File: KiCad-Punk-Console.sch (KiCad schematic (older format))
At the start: 5 parts

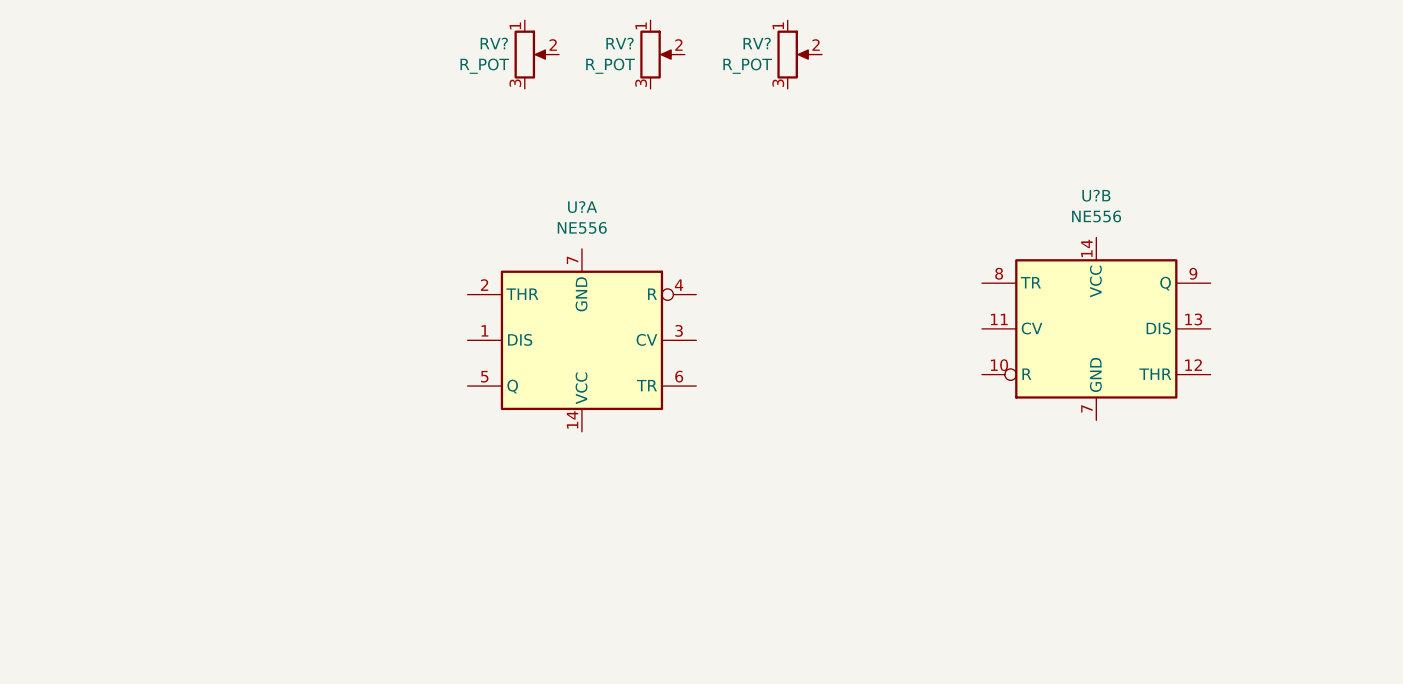
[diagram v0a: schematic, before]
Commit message: placed symbols
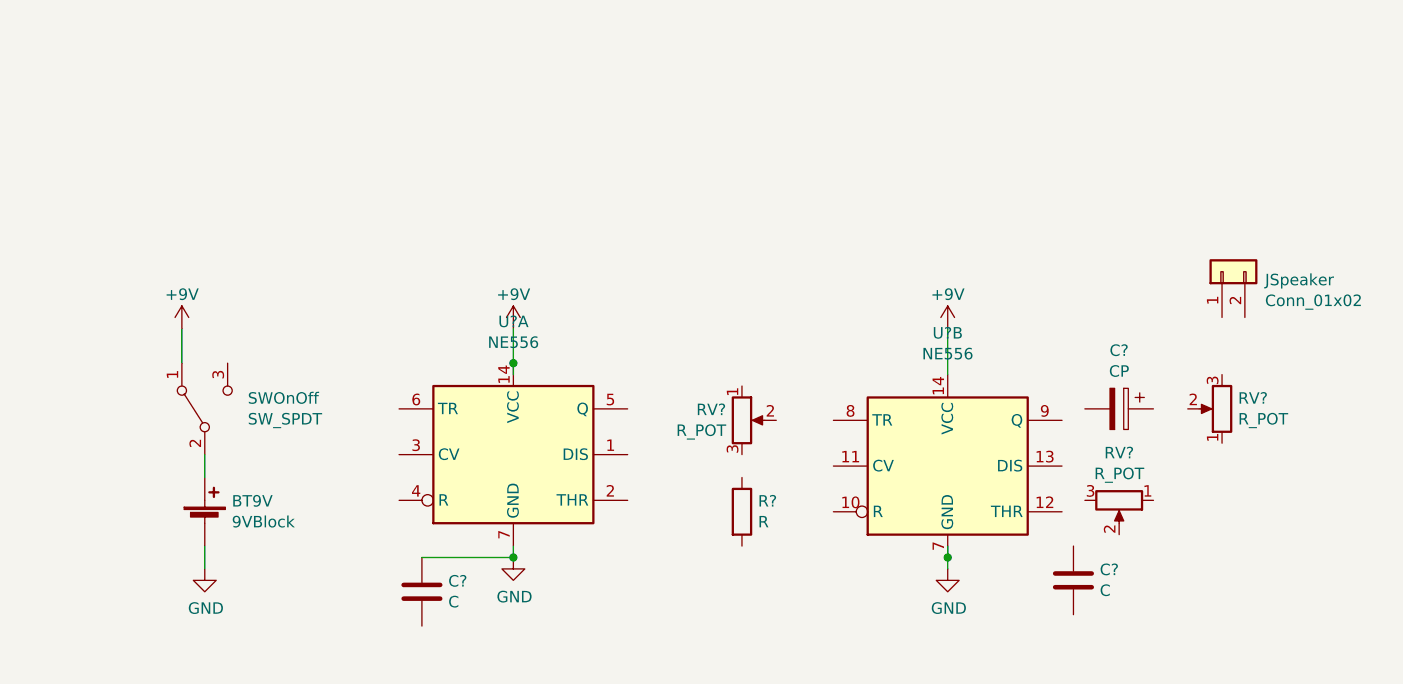
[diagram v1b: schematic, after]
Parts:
- added BT9V: 9VBlock, symbol Device:Battery_Cell
- added C? (x2): C, symbol Device:C
- added C?: CP, symbol Device:CP
- added JSpeaker: Conn_01x02, symbol Connector_Generic:Conn_01x02
- added R?: R, symbol Device:R
- added SWOnOff: SW_SPDT, symbol Switch:SW_SPDT
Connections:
- net labels added: +9V, GND
- wire segments 0 -> 10
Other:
- moved on the sheet: RV?, U?A, U?B
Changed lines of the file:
@@
 L Timer:NE556 U?
 U 1 1 5D8120BC
-P 5100 3000
-F 0 "U?" H 5100 2419 50  0000 C CNN
-F 1 "NE556" H 5100 2510 50  0000 C CNN
-F 2 "" H 5100 3000 50  0001 C CNN
-F 3 "http://www.ti.com/lit/ds/symlink/ne556.pdf" H 5100 3000 50  0001 C CNN
-	1    5100 3000
-	-1   0    0    1
+P 4800 3500
+F 0 "U?" H 4800 4081 50  0000 C CNN
+F 1 "NE556" H 4800 3990 50  0000 C CNN
+F 2 "" H 4800 3500 50  0001 C CNN
+F 3 "http://www.ti.com/lit/ds/symlink/ne556.pdf" H 4800 3500 50  0001 C CNN
+	1    4800 3500
+	1    0    0    -1
 $EndComp
 $Comp
 L Timer:NE556 U?
 U 2 1 5D81293A
-P 7350 2950
-F 0 "U?" H 7350 3531 50  0000 C CNN
-F 1 "NE556" H 7350 3440 50  0000 C CNN
-F 2 "" H 7350 2950 50  0001 C CNN
-F 3 "http://www.ti.com/lit/ds/symlink/ne556.pdf" H 7350 2950 50  0001 C CNN
-	2    7350 2950
+P 6700 3550
+F 0 "U?" H 6700 4131 50  0000 C CNN
+F 1 "NE556" H 6700 4040 50  0000 C CNN
+F 2 "" H 6700 3550 50  0001 C CNN
+F 3 "http://www.ti.com/lit/ds/symlink/ne556.pdf" H 6700 3550 50  0001 C CNN
+	2    6700 3550
 	1    0    0    -1
 $EndComp
@@
 L Device:R_POT RV?
 U 1 1 5D8204BB
-P 4850 1750
-F 0 "RV?" H 4781 1796 50  0000 R CNN
-F 1 "R_POT" H 4781 1705 50  0000 R CNN
-F 2 "" H 4850 1750 50  0001 C CNN
-F 3 "~" H 4850 1750 50  0001 C CNN
-	1    4850 1750
+P 5800 3350
+F 0 "RV?" H 5731 3396 50  0000 R CNN
+F 1 "R_POT" H 5731 3305 50  0000 R CNN
+F 2 "" H 5800 3350 50  0001 C CNN
+F 3 "~" H 5800 3350 50  0001 C CNN
+	1    5800 3350
 	1    0    0    -1
 $EndComp
@@
 L Device:R_POT RV?
 U 1 1 5D821740
-P 5400 1750
-F 0 "RV?" H 5331 1796 50  0000 R CNN
-F 1 "R_POT" H 5331 1705 50  0000 R CNN
-F 2 "" H 5400 1750 50  0001 C CNN
-F 3 "~" H 5400 1750 50  0001 C CNN
-	1    5400 1750
-	1    0    0    -1
+P 7900 3300
+F 0 "RV?" H 7830 3254 50  0000 R CNN
+F 1 "R_POT" H 7830 3345 50  0000 R CNN
+F 2 "" H 7900 3300 50  0001 C CNN
+F 3 "~" H 7900 3300 50  0001 C CNN
+	1    7900 3300
+	-1   0    0    1
 $EndComp
 $Comp
 L Device:R_POT RV?
 U 1 1 5D8219B1
-P 6000 1750
-F 0 "RV?" H 5931 1796 50  0000 R CNN
-F 1 "R_POT" H 5931 1705 50  0000 R CNN
-F 2 "" H 6000 1750 50  0001 C CNN
-F 3 "~" H 6000 1750 50  0001 C CNN
-	1    6000 1750
-	1    0    0    -1
-$EndComp
+P 7450 3700
+F 0 "RV?" V 7243 3700 50  0000 C CNN
+F 1 "R_POT" V 7334 3700 50  0000 C CNN
+F 2 "" H 7450 3700 50  0001 C CNN
+F 3 "~" H 7450 3700 50  0001 C CNN
+	1    7450 3700
+	0    1    1    0
+$EndComp
+$Comp
+L Device:R R?
+U 1 1 5D8233A2
+P 5800 3750
+F 0 "R?" H 5870 3796 50  0000 L CNN
+F 1 "R" H 5870 3705 50  0000 L CNN
+F 2 "" V 5730 3750 50  0001 C CNN
+F 3 "~" H 5800 3750 50  0001 C CNN
+	1    5800 3750
+	1    0    0    -1
+$EndComp
+$Comp
+L Device:C C?
+U 1 1 5D824169
+P 7250 4050
+F 0 "C?" H 7365 4096 50  0000 L CNN
+F 1 "C" H 7365 4005 50  0000 L CNN
+F 2 "" H 7288 3900 50  0001 C CNN
+F 3 "~" H 7250 4050 50  0001 C CNN
+	1    7250 4050
+	1    0    0    -1
+$EndComp
+$Comp
+L Device:C C?
+U 1 1 5D824752
+P 4400 4100
+F 0 "C?" H 4515 4146 50  0000 L CNN
+F 1 "C" H 4515 4055 50  0000 L CNN
+F 2 "" H 4438 3950 50  0001 C CNN
+F 3 "~" H 4400 4100 50  0001 C CNN
+	1    4400 4100
+	1    0    0    -1
+$EndComp
+$Comp
+L Device:CP C?
+U 1 1 5D82504C
+P 7450 3300
+F 0 "C?" V 7195 3300 50  0000 C CNN
+F 1 "CP" V 7286 3300 50  0000 C CNN
+F 2 "" H 7488 3150 50  0001 C CNN
+F 3 "~" H 7450 3300 50  0001 C CNN
+	1    7450 3300
+	0    1    1    0
+$EndComp
+$Comp
+L Device:Battery_Cell BT9V
+U 1 1 5D826185
+P 3450 3800
+F 0 "BT9V" H 3568 3896 50  0000 L CNN
+F 1 "9VBlock" H 3568 3805 50  0000 L CNN
+F 2 "" V 3450 3860 50  0001 C CNN
+F 3 "~" V 3450 3860 50  0001 C CNN
+	1    3450 3800
+	1    0    0    -1
+$EndComp
+$Comp
+L Connector_Generic:Conn_01x02 JSpeaker
+U 1 1 5D829AFF
+P 7900 2700
+F 0 "JSpeaker" V 7864 2512 50  0000 R CNN
+F 1 "Conn_01x02" V 7773 2512 50  0000 R CNN
+F 2 "" H 7900 2700 50  0001 C CNN
+F 3 "~" H 7900 2700 50  0001 C CNN
+	1    7900 2700
+	0    -1   -1   0
+$EndComp
+$Comp
+L Switch:SW_SPDT SWOnOff
+U 1 1 5D82C32B
+P 3450 3300
+F 0 "SWOnOff" V 3496 3112 50  0000 R CNN
+F 1 "SW_SPDT" V 3405 3112 50  0000 R CNN
+F 2 "" H 3450 3300 50  0001 C CNN
+F 3 "~" H 3450 3300 50  0001 C CNN
+	1    3450 3300
+	0    -1   -1   0
+$EndComp
+Wire Wire Line
+	3450 3500 3450 3600
+$Comp
+L power:+9V #PWR?
+U 1 1 5D84CF30
+P 3350 2950
+F 0 "#PWR?" H 3350 2800 50  0001 C CNN
+F 1 "+9V" H 3350 3100 50  0000 C CNN
+F 2 "" H 3350 2950 50  0001 C CNN
+F 3 "" H 3350 2950 50  0001 C CNN
+	1    3350 2950
+	1    0    0    -1
+$EndComp
+Wire Wire Line
+	3350 2950 3350 3100
+$Comp
+L power:GND #PWR?
+U 1 1 5D84DD18
+P 3450 4000
+F 0 "#PWR?" H 3450 3750 50  0001 C CNN
+F 1 "GND" H 3455 3827 50  0000 C CNN
+F 2 "" H 3450 4000 50  0001 C CNN
+F 3 "" H 3450 4000 50  0001 C CNN
+	1    3450 4000
+	1    0    0    -1
+$EndComp
+Wire Wire Line
+	3450 4000 3450 3900
+$Comp
+L power:GND #PWR?
+U 1 1 5D84E572
+P 4800 3950
+F 0 "#PWR?" H 4800 3700 50  0001 C CNN
+F 1 "GND" H 4805 3777 50  0000 C CNN
+F 2 "" H 4800 3950 50  0001 C CNN
+F 3 "" H 4800 3950 50  0001 C CNN
+	1    4800 3950
+	1    0    0    -1
+$EndComp
+$Comp
+L power:GND #PWR?
+U 1 1 5D84EDE7
+P 6700 4000
+F 0 "#PWR?" H 6700 3750 50  0001 C CNN
+F 1 "GND" H 6705 3827 50  0000 C CNN
+F 2 "" H 6700 4000 50  0001 C CNN
+F 3 "" H 6700 4000 50  0001 C CNN
+	1    6700 4000
+	1    0    0    -1
+$EndComp
+Wire Wire Line
+	6700 3900 6700 3950
+Connection ~ 6700 3950
+Wire Wire Line
+	6700 3950 6700 4000
+$Comp
+L power:+9V #PWR?
+U 1 1 5D850507
+P 4800 2950
+F 0 "#PWR?" H 4800 2800 50  0001 C CNN
+F 1 "+9V" H 4800 3100 50  0000 C CNN
+F 2 "" H 4800 2950 50  0001 C CNN
+F 3 "" H 4800 2950 50  0001 C CNN
+	1    4800 2950
+	1    0    0    -1
+$EndComp
+$Comp
+L power:+9V #PWR?
+U 1 1 5D8519A0
+P 6700 2950
+F 0 "#PWR?" H 6700 2800 50  0001 C CNN
+F 1 "+9V" H 6700 3100 50  0000 C CNN
+F 2 "" H 6700 2950 50  0001 C CNN
+F 3 "" H 6700 2950 50  0001 C CNN
+	1    6700 2950
+	1    0    0    -1
+$EndComp
+Wire Wire Line
+	4800 2950 4800 3100
+Wire Wire Line
+	6700 2950 6700 3150
+Connection ~ 4800 3100
+Wire Wire Line
+	4800 3100 4800 3150
+Wire Wire Line
+	4800 3900 4800 3950
+Wire Wire Line
+	4400 3950 4800 3950
+Connection ~ 4800 3950
 $EndSCHEMATC

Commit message: wired symbols
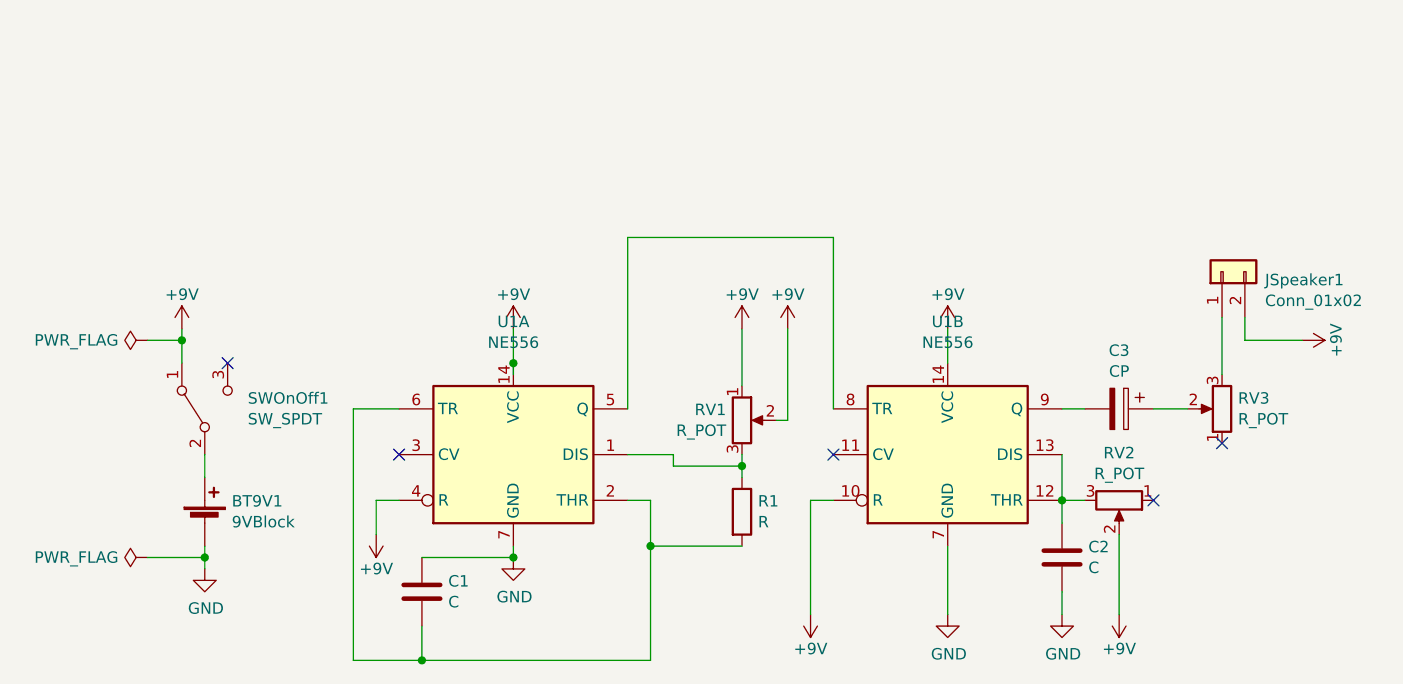
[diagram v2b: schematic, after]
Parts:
- gave numbers to parts that had none: 8
- renumbered BT9V to BT9V1, JSpeaker to JSpeaker1, SWOnOff to SWOnOff1
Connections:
- wire segments 10 -> 47
- no-connect marks 0 -> 5
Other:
- moved on the sheet: C2, U1B

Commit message: added values to symbols
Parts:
- BT9V1: value 9VBlock -> 9V
- C1: value C -> 10nF
- C2: value C -> 100nF
- C3: value CP -> 10uF
- JSpeaker1: value Conn_01x02 -> Speaker
- R1: value R -> 1k
- RV1, RV2: value R_POT -> 1M
- RV3: value R_POT -> 5k
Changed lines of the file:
@@
 P 5800 3350
 F 0 "RV1" H 5731 3396 50  0000 R CNN
-F 1 "R_POT" H 5731 3305 50  0000 R CNN
+F 1 "1M" H 5731 3305 50  0000 R CNN
 F 2 "" H 5800 3350 50  0001 C CNN
 F 3 "~" H 5800 3350 50  0001 C CNN
@@
 P 7900 3300
 F 0 "RV3" H 7830 3254 50  0000 R CNN
-F 1 "R_POT" H 7830 3345 50  0000 R CNN
+F 1 "5k" H 7830 3345 50  0000 R CNN
 F 2 "" H 7900 3300 50  0001 C CNN
 F 3 "~" H 7900 3300 50  0001 C CNN
@@
 P 7450 3700
 F 0 "RV2" V 7243 3700 50  0000 C CNN
-F 1 "R_POT" V 7334 3700 50  0000 C CNN
+F 1 "1M" V 7334 3700 50  0000 C CNN
 F 2 "" H 7450 3700 50  0001 C CNN
 F 3 "~" H 7450 3700 50  0001 C CNN
@@
 P 5800 3750
 F 0 "R1" H 5870 3796 50  0000 L CNN
-F 1 "R" H 5870 3705 50  0000 L CNN
+F 1 "1k" H 5870 3705 50  0000 L CNN
 F 2 "" V 5730 3750 50  0001 C CNN
 F 3 "~" H 5800 3750 50  0001 C CNN
@@
 P 7200 3950
 F 0 "C2" H 7315 3996 50  0000 L CNN
-F 1 "C" H 7315 3905 50  0000 L CNN
+F 1 "100nF" H 7315 3905 50  0000 L CNN
 F 2 "" H 7238 3800 50  0001 C CNN
 F 3 "~" H 7200 3950 50  0001 C CNN
@@
 P 4400 4100
 F 0 "C1" H 4515 4146 50  0000 L CNN
-F 1 "C" H 4515 4055 50  0000 L CNN
+F 1 "10nF" H 4515 4055 50  0000 L CNN
 F 2 "" H 4438 3950 50  0001 C CNN
 F 3 "~" H 4400 4100 50  0001 C CNN
@@
 P 7450 3300
 F 0 "C3" V 7195 3300 50  0000 C CNN
-F 1 "CP" V 7286 3300 50  0000 C CNN
+F 1 "10uF" V 7286 3300 50  0000 C CNN
 F 2 "" H 7488 3150 50  0001 C CNN
 F 3 "~" H 7450 3300 50  0001 C CNN
@@
 P 3450 3800
 F 0 "BT9V1" H 3568 3896 50  0000 L CNN
-F 1 "9VBlock" H 3568 3805 50  0000 L CNN
+F 1 "9V" H 3568 3805 50  0000 L CNN
 F 2 "" V 3450 3860 50  0001 C CNN
 F 3 "~" V 3450 3860 50  0001 C CNN
@@
 P 7900 2700
 F 0 "JSpeaker1" V 7864 2512 50  0000 R CNN
-F 1 "Conn_01x02" V 7773 2512 50  0000 R CNN
+F 1 "Speaker" V 7773 2512 50  0000 R CNN
 F 2 "" H 7900 2700 50  0001 C CNN
 F 3 "~" H 7900 2700 50  0001 C CNN
@@
 	4400 4400 5400 4400
 $Comp
-L power:PWR_FLAG #FLG?
+L power:PWR_FLAG #FLG0101
 U 1 1 5D871906
 P 3200 3000
-F 0 "#FLG?" H 3200 3075 50  0001 C CNN
+F 0 "#FLG0101" H 3200 3075 50  0001 C CNN
 F 1 "PWR_FLAG" V 3200 3127 50  0000 L CNN
 F 2 "" H 3200 3000 50  0001 C CNN
@@
 	3350 3000 3350 3100
 $Comp
-L power:PWR_FLAG #FLG?
+L power:PWR_FLAG #FLG0102
 U 1 1 5D872E21
 P 3200 3950
-F 0 "#FLG?" H 3200 4025 50  0001 C CNN
+F 0 "#FLG0102" H 3200 4025 50  0001 C CNN
 F 1 "PWR_FLAG" V 3200 4077 50  0000 L CNN
 F 2 "" H 3200 3950 50  0001 C CNN

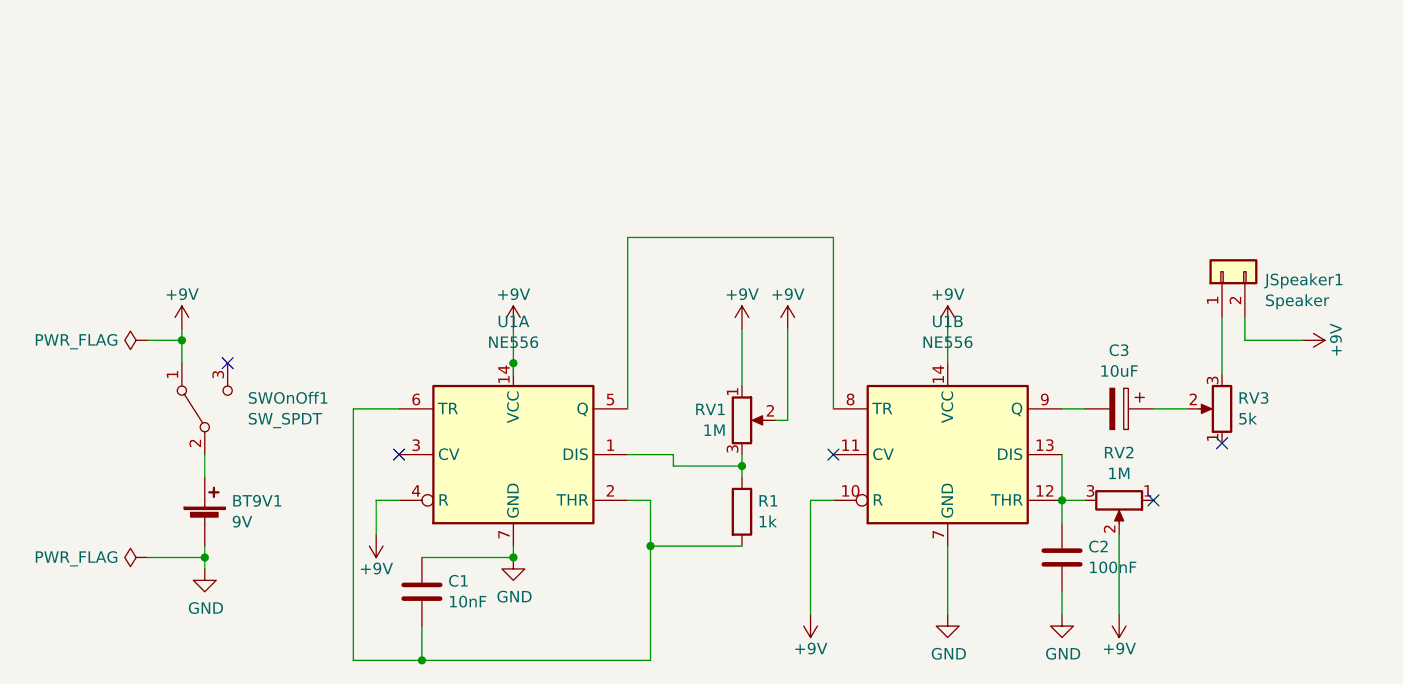
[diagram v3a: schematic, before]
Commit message: addded test points
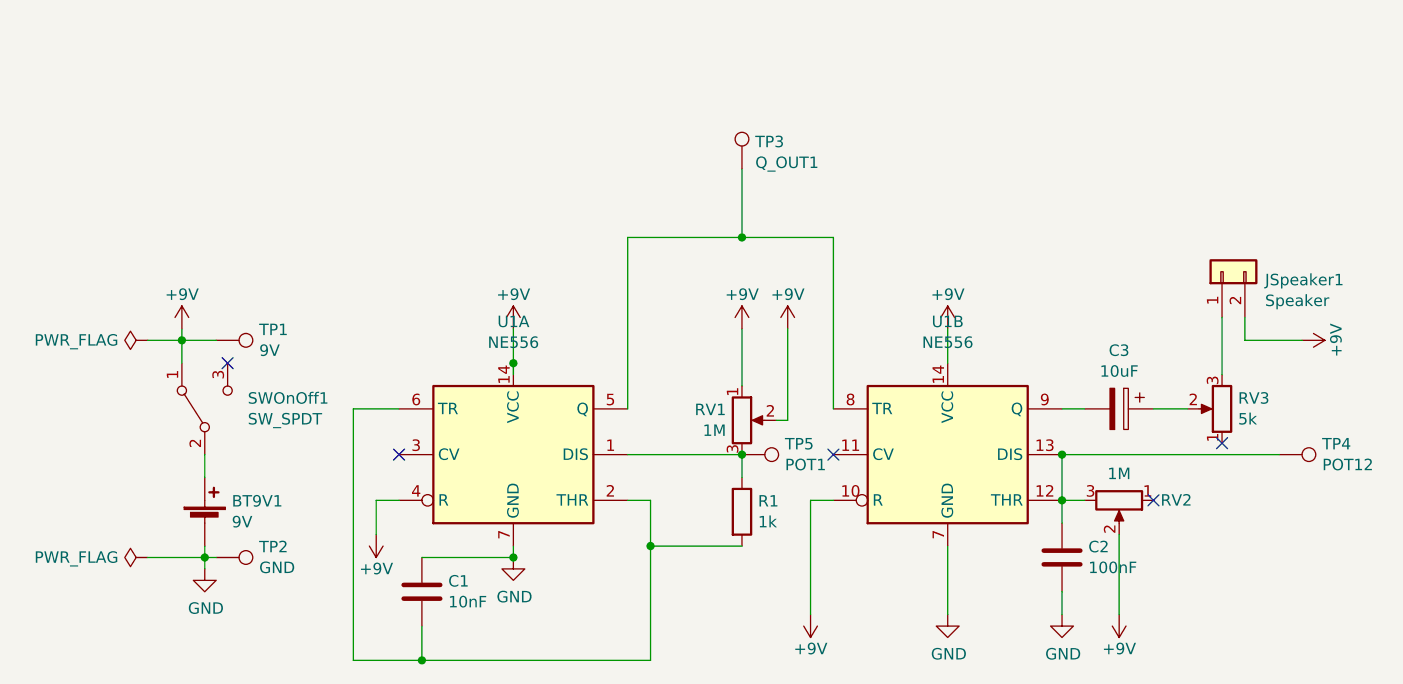
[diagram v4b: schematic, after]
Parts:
- added TP1: 9V, symbol Connector:TestPoint
- added TP2: GND, symbol Connector:TestPoint
- added TP3: Q_OUT1, symbol Connector:TestPoint
- added TP4: POT12, symbol Connector:TestPoint
- added TP5: POT1, symbol Connector:TestPoint
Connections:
- net +9V: now also TP1.1
- net GND: now also TP2.1
- net at R1.1, RV1.3, U1.1 (DIS): now also TP5.1
- net at U1.5 (Q), U1.8 (TR): now also TP3.1
- net at C2.1, RV2.3, U1.12 (THR)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: now also TP4.1
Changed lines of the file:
@@
 U 1 1 5D8219B1
 P 7450 3700
-F 0 "RV2" V 7243 3700 50  0000 C CNN
+F 0 "RV2" V 7450 3950 50  0000 C CNN
 F 1 "1M" V 7334 3700 50  0000 C CNN
 F 2 "" H 7450 3700 50  0001 C CNN
@@
 	5400 3900 5400 3700
 Wire Wire Line
-	5800 3600 5800 3550
-Wire Wire Line
-	5300 3500 5500 3500
-Wire Wire Line
-	5500 3500 5500 3550
-Wire Wire Line
-	5500 3550 5800 3550
-Connection ~ 5800 3550
-Wire Wire Line
-	5800 3550 5800 3500
+	5800 3600 5800 3500
+Connection ~ 5800 3500
 $Comp
 L power:+9V #PWR0107
@@
 	5300 3300 5300 2550
 Wire Wire Line
-	5300 2550 6200 2550
+	5300 2550 5800 2550
 Wire Wire Line
 	6200 2550 6200 3300
@@
 Wire Wire Line
 	3450 3950 3450 3900
+$Comp
+L Connector:TestPoint TP1
+U 1 1 5D8767BF
+P 3500 3000
+F 0 "TP1" V 3454 3188 50  0000 L CNN
+F 1 "9V" V 3545 3188 50  0000 L CNN
+F 2 "" H 3700 3000 50  0001 C CNN
+F 3 "~" H 3700 3000 50  0001 C CNN
+	1    3500 3000
+	0    1    1    0
+$EndComp
+Wire Wire Line
+	3350 3000 3500 3000
+$Comp
+L Connector:TestPoint TP2
+U 1 1 5D87812C
+P 3500 3950
+F 0 "TP2" V 3454 4138 50  0000 L CNN
+F 1 "GND" V 3545 4138 50  0000 L CNN
+F 2 "" H 3700 3950 50  0001 C CNN
+F 3 "~" H 3700 3950 50  0001 C CNN
+	1    3500 3950
+	0    1    1    0
+$EndComp
+Wire Wire Line
+	3500 3950 3450 3950
+$Comp
+L Connector:TestPoint TP4
+U 1 1 5D879CCC
+P 8150 3500
+F 0 "TP4" V 8104 3688 50  0000 L CNN
+F 1 "POT12" V 8195 3688 50  0000 L CNN
+F 2 "" H 8350 3500 50  0001 C CNN
+F 3 "~" H 8350 3500 50  0001 C CNN
+	1    8150 3500
+	0    1    1    0
+$EndComp
+Wire Wire Line
+	8150 3500 7200 3500
+Connection ~ 7200 3500
+$Comp
+L Connector:TestPoint TP3
+U 1 1 5D87D867
+P 5800 2250
+F 0 "TP3" H 5858 2368 50  0000 L CNN
+F 1 "Q_OUT1" H 5858 2277 50  0000 L CNN
+F 2 "" H 6000 2250 50  0001 C CNN
+F 3 "~" H 6000 2250 50  0001 C CNN
+	1    5800 2250
+	1    0    0    -1
+$EndComp
+Wire Wire Line
+	5800 2250 5800 2550
+Connection ~ 5800 2550
+Wire Wire Line
+	5800 2550 6200 2550
+$Comp
+L Connector:TestPoint TP5
+U 1 1 5D87F49A
+P 5800 3500
+F 0 "TP5" V 5754 3688 50  0000 L CNN
+F 1 "POT1" V 5845 3688 50  0000 L CNN
+F 2 "" H 6000 3500 50  0001 C CNN
+F 3 "~" H 6000 3500 50  0001 C CNN
+	1    5800 3500
+	0    1    1    0
+$EndComp
+Wire Wire Line
+	5300 3500 5800 3500
 $EndSCHEMATC
